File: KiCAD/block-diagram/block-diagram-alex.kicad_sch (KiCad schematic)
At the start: 34 parts, among them J1 Conn_01x08, J2 Conn_01x08, J3 Conn_01x10, Q3 NMOS, Q4 NMOS, U1 74LS02, U3 74LS11, U6 LMC555xM

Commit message: Grounded, open pin of the 555
There was a pin of the 555 that was connected to nothing, I connected it to ground, not sure if this is correct, but I believe generally that's what we are doing for unconnected pins, not sure if that one served a purpose though.
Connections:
- net GND: now also U6.5 (CV)
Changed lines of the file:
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@@
 	(wire
 		(pts
+			(xy 176.53 43.18) (xy 182.88 43.18)
+		)
+		(stroke
+			(width 0)
+			(type default)
+		)
+	)
+	(wire
+		(pts
 			(xy 115.57 102.87) (xy 215.9 102.87)
 		)
@@
 					(unit 1)
 				)
+			)
+		)
+	)
+	(symbol
+		(lib_id "power:GND")
+		(at 176.53 43.18 0)
+		(unit 1)
+		(exclude_from_sim no)
+		(in_bom yes)
+		(on_board yes)
+		(dnp no)
+		(fields_autoplaced yes)
+		(property "Reference" "#PWR029"
+			(at 176.53 49.53 0)
+			(effects
+				(font
+					(size 1.27 1.27)
+				)
+				(hide yes)
+			)
+		)
+		(property "Value" "GND"
+			(at 176.53 48.26 0)
+			(effects
+				(font
+					(size 1.27 1.27)
+				)
+			)
+		)
+		(property "Footprint" ""
+			(at 176.53 43.18 0)
+			(effects
+				(font
+					(size 1.27 1.27)
+				)
+				(hide yes)
+			)
+		)
+		(property "Datasheet" ""
+			(at 176.53 43.18 0)
+			(effects
+				(font
+					(size 1.27 1.27)
+				)
+				(hide yes)
+			)
+		)
+		(property "Description" "Power symbol creates a global label with name \"GND\" , ground"
+			(at 176.53 43.18 0)
+			(effects
+				(font
+					(size 1.27 1.27)
+				)
+				(hide yes)
+			)
+		)
+		(pin "1"
+		)
+		(instances
+			(project "block-diagram-alex"
+				(path "/db38bfac-663c-442a-8ac2-f7bf1aa9a3fd"
+					(reference "#PWR029")
+					(unit 1)
+				)

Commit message: Start filling symbol attributes; move J2 a bit
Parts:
- C4: CatNo (none) -> 4713-GMC21X5R106J10NTCT-ND; MfgNo (none) -> GMC21X5R106J10NT
- Q3, Q4: CatNo (none) -> DMN2046U-7DICT-ND; MfgNo (none) -> DMN2046U-7
- U6: CatNo (none) -> LM555CMX/NOPBCT-ND; MfgNo (none) -> LM555CMX/NOPB
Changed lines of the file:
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@@
 		(on_board yes)
 		(dnp no)
-		(fields_autoplaced yes)
 		(property "Reference" "U6"
 			(at 197.7741 30.48 0)
@@
 			)
 		)
+		(property "CatNo" "LM555CMX/NOPBCT-ND"
+			(at 180.848 53.086 0)
+			(effects
+				(font
+					(size 1.27 1.27)
+				)
+			)
+		)
+		(property "MfgNo" "LM555CMX/NOPB"
+			(at 195.58 43.18 0)
+			(effects
+				(font
+					(size 1.27 1.27)
+				)
+				(hide yes)
+			)
+		)
 		(pin "8"
 		)
@@
 			)
 		)
+		(property "CatNo" "DMN2046U-7DICT-ND"
+			(at 187.96 67.31 0)
+			(effects
+				(font
+					(size 1.27 1.27)
+				)
+				(hide yes)
+			)
+		)
+		(property "MfgNo" "DMN2046U-7"
+			(at 187.96 67.31 0)
+			(effects
+				(font
+					(size 1.27 1.27)
+				)
+				(hide yes)
+			)
+		)
 		(pin "1"
 		)
@@
 		(on_board yes)
 		(dnp no)
-		(fields_autoplaced yes)
 		(property "Reference" "C4"
 			(at 214.63 63.5062 0)
@@
 			)
 		)
+		(property "CatNo" "4713-GMC21X5R106J10NTCT-ND"
+			(at 230.378 68.58 0)
+			(effects
+				(font
+					(size 1.27 1.27)
+				)
+			)
+		)
+		(property "MfgNo" "GMC21X5R106J10NT"
+			(at 212.09 64.77 0)
+			(effects
+				(font
+					(size 1.27 1.27)
+				)
+				(hide yes)
+			)
+		)
 		(pin "2"
 		)
@@
 		(on_board yes)
 		(dnp no)
-		(fields_autoplaced yes)
 		(property "Reference" "Q3"
 			(at 173.99 66.0399 0)
@@
 			(effects
 				(font
+					(size 1.27 1.27)
+				)
+				(hide yes)
+			)
+		)
+		(property "CatNo" "DMN2046U-7DICT-ND"
+			(at 157.226 71.628 0)
+			(effects
+				(font
+					(size 1.27 1.27)
+				)
+			)
+		)
+		(property "MfgNo" "DMN2046U-7"
+			(at 167.64 67.31 0)
+			(effects
+				(font

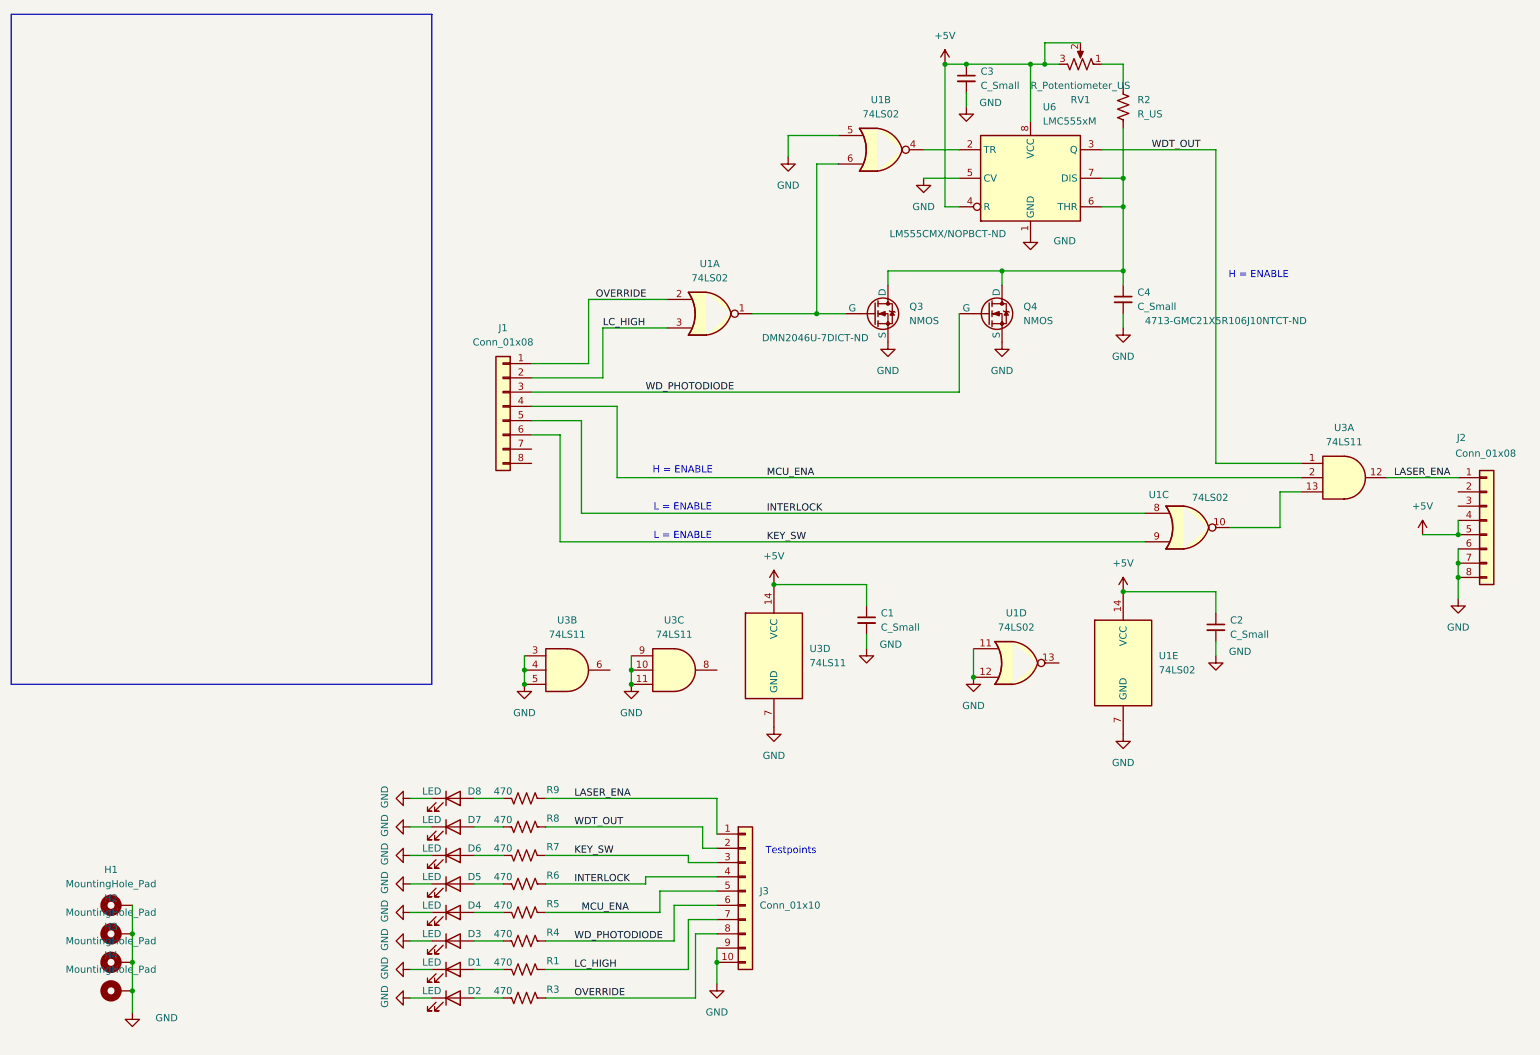
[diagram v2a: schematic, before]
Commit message: Finishing Touches before adding Part and Cfg Nums
*  Fix silkscreen text overlaps
*  Move J2 up or down .05" and fix routing
*  Disconnect 555 pin 5 from GND and add a 10uF capacitor
*  Change U1, U3 from 74LS--- to 74HC---
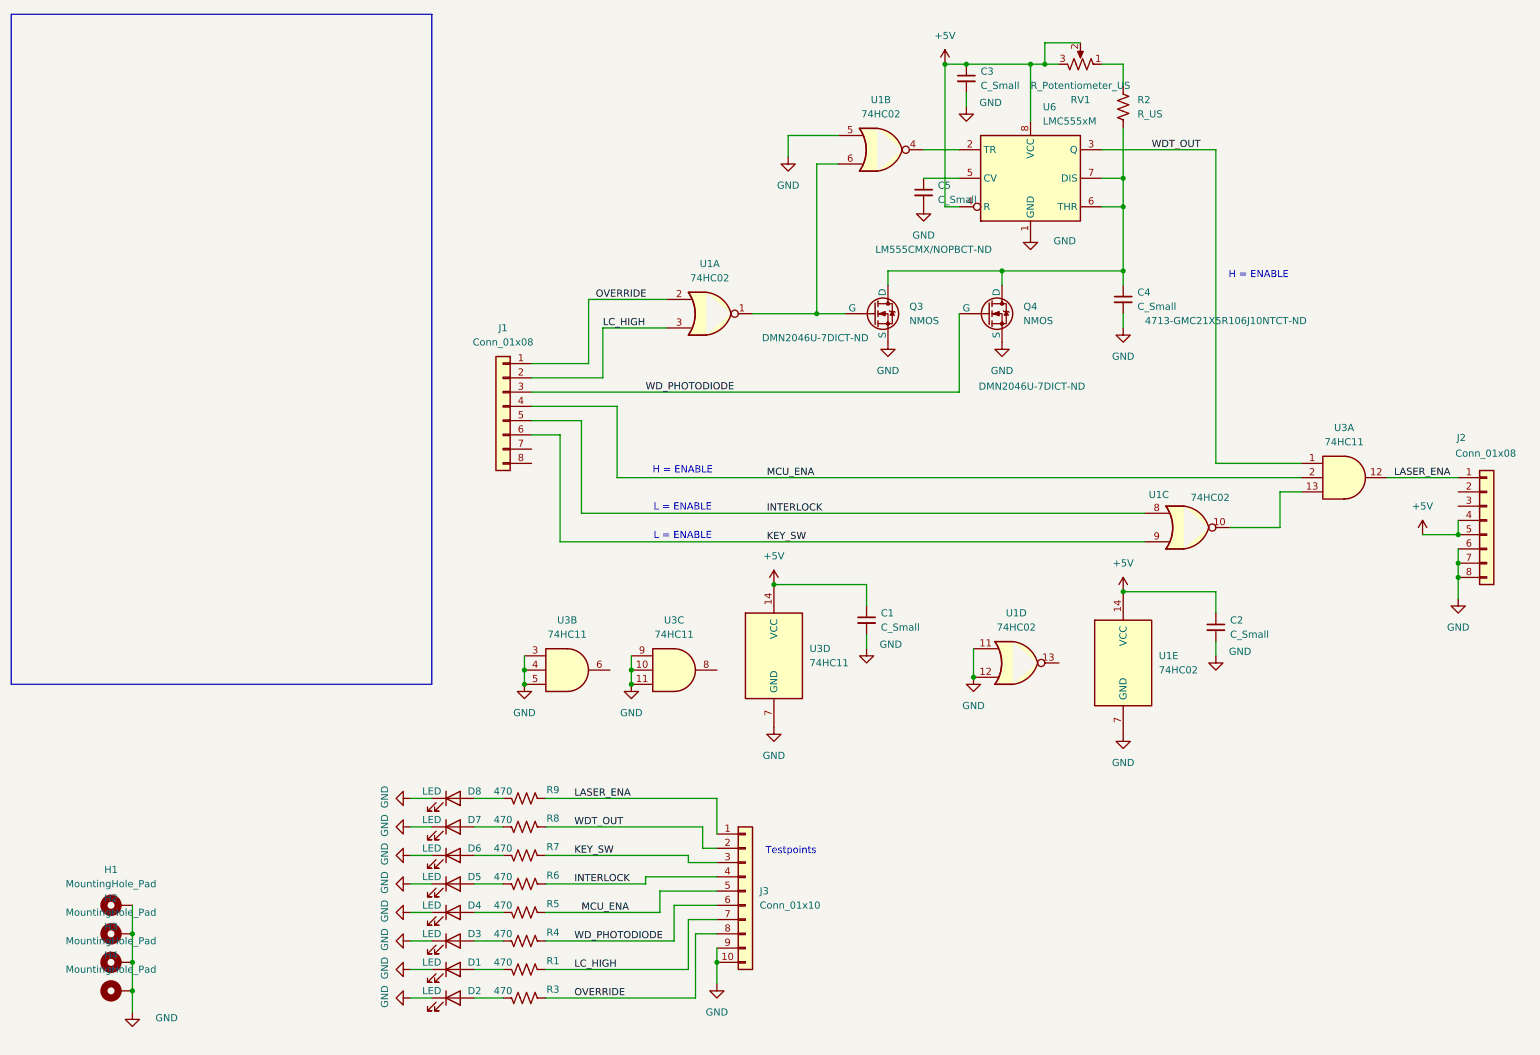
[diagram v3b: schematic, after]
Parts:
- added C5: C_Small, Capacitor_SMD:C_0805_2012Metric_Pad1.18x1.45mm_HandSolder, symbol Device:C_Small
- U1: value 74LS02 -> 74HC02
- U3: value 74LS11 -> 74HC11
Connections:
- net GND: now also C5.2; no longer U6.5 (CV)
- new net: C5.1, U6.5 (CV)
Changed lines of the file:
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@@
 			)
 		)
-		(property "Value" "74LS02"
+		(property "Value" "74HC02"
 			(at 168.91 31.75 0)
 			(effects
@@
 		)
 		(property "CatNo" "LM555CMX/NOPBCT-ND"
-			(at 180.848 53.086 0)
+			(at 178.308 55.88 0)
 			(effects
 				(font
@@
 			)
 		)
-		(property "Value" "74LS02"
+		(property "Value" "74HC02"
 			(at 227.584 100.076 0)
 			(effects
@@
 			)
 		)
-		(property "Value" "74LS02"
+		(property "Value" "74HC02"
 			(at 138.43 60.96 0)
 			(effects
@@
 			)
 		)
-		(property "Value" "74LS11"
+		(property "Value" "74HC11"
 			(at 132.0717 124.46 0)
 			(effects
@@
 	(symbol
 		(lib_id "Device:C_Small")
+		(at 176.53 45.72 0)
+		(unit 1)
+		(exclude_from_sim no)
+		(in_bom yes)
+		(on_board yes)
+		(dnp no)
+		(fields_autoplaced yes)
+		(property "Reference" "C5"
+			(at 179.07 44.4562 0)
+			(effects
+				(font
+					(size 1.27 1.27)
+				)
+				(justify left)
+			)
+		)
+		(property "Value" "C_Small"
+			(at 179.07 46.9962 0)
+			(effects
+				(font
+					(size 1.27 1.27)
+				)
+				(justify left)
+			)
+		)
+		(property "Footprint" "Capacitor_SMD:C_0805_2012Metric_Pad1.18x1.45mm_HandSolder"
+			(at 176.53 45.72 0)
+			(effects
+				(font
+					(size 1.27 1.27)
+				)
+				(hide yes)
+			)
+		)
+		(property "Datasheet" "~"
+			(at 176.53 45.72 0)
+			(effects
+				(font
+					(size 1.27 1.27)
+				)
+				(hide yes)
+			)
+		)
+		(property "Description" "Unpolarized capacitor, small symbol"
+			(at 176.53 45.72 0)
+			(effects
+				(font
+					(size 1.27 1.27)
+				)
+				(hide yes)
+			)
+		)
+		(pin "1"
+		)
+		(pin "2"
+		)
+		(instances
+			(project "block-diagram-alex"
+				(path "/db38bfac-663c-442a-8ac2-f7bf1aa9a3fd"
+					(reference "C5")
+					(unit 1)
+				)
+			)
+		)
+	)
+	(symbol
+		(lib_id "Device:C_Small")
 		(at 228.6 123.19 0)
 		(unit 1)
@@
 	(symbol
 		(lib_id "power:GND")
-		(at 176.53 43.18 0)
+		(at 176.53 48.26 0)
 		(unit 1)
 		(exclude_from_sim no)
@@
 		(fields_autoplaced yes)
 		(property "Reference" "#PWR029"
-			(at 176.53 49.53 0)
+			(at 176.53 54.61 0)
 			(effects
 				(font
@@
 		)
 		(property "Value" "GND"
-			(at 176.53 48.26 0)
+			(at 176.53 53.34 0)
 			(effects
 				(font
@@
 		)
 		(property "Footprint" ""
-			(at 176.53 43.18 0)
+			(at 176.53 48.26 0)
 			(effects
 				(font
@@
 		)
 		(property "Datasheet" ""
-			(at 176.53 43.18 0)
+			(at 176.53 48.26 0)
 			(effects
 				(font
@@
 		)
 		(property "Description" "Power symbol creates a global label with name \"GND\" , ground"
-			(at 176.53 43.18 0)
+			(at 176.53 48.26 0)
 			(effects
 				(font
@@
 			)
 		)
-		(property "Value" "74LS02"
+		(property "Value" "74HC02"
 			(at 193.04 123.19 0)
 			(effects
@@
 			)
 		)
-		(property "Value" "74LS02"
+		(property "Value" "74HC02"
 			(at 218.44 130.8099 0)
 			(effects
@@
 			)
 		)
-		(property "Value" "74LS11"
+		(property "Value" "74HC11"
 			(at 251.4517 90.17 0)
 			(effects
@@
 		(on_board yes)
 		(dnp no)
-		(fields_autoplaced yes)
 		(property "Reference" "Q4"
 			(at 194.31 66.0399 0)
@@
 		)
 		(property "CatNo" "DMN2046U-7DICT-ND"
-			(at 187.96 67.31 0)
+			(at 195.834 80.264 0)
 			(effects
 				(font
 					(size 1.27 1.27)
 				)
-				(hide yes)
 			)
 		)
@@
 			)
 		)
-		(property "Value" "74LS11"
+		(property "Value" "74HC11"
 			(at 113.0217 124.46 0)
 			(effects
@@
 			)
 		)
-		(property "Value" "74LS11"
+		(property "Value" "74HC11"
 			(at 156.21 129.5399 0)
 			(effects

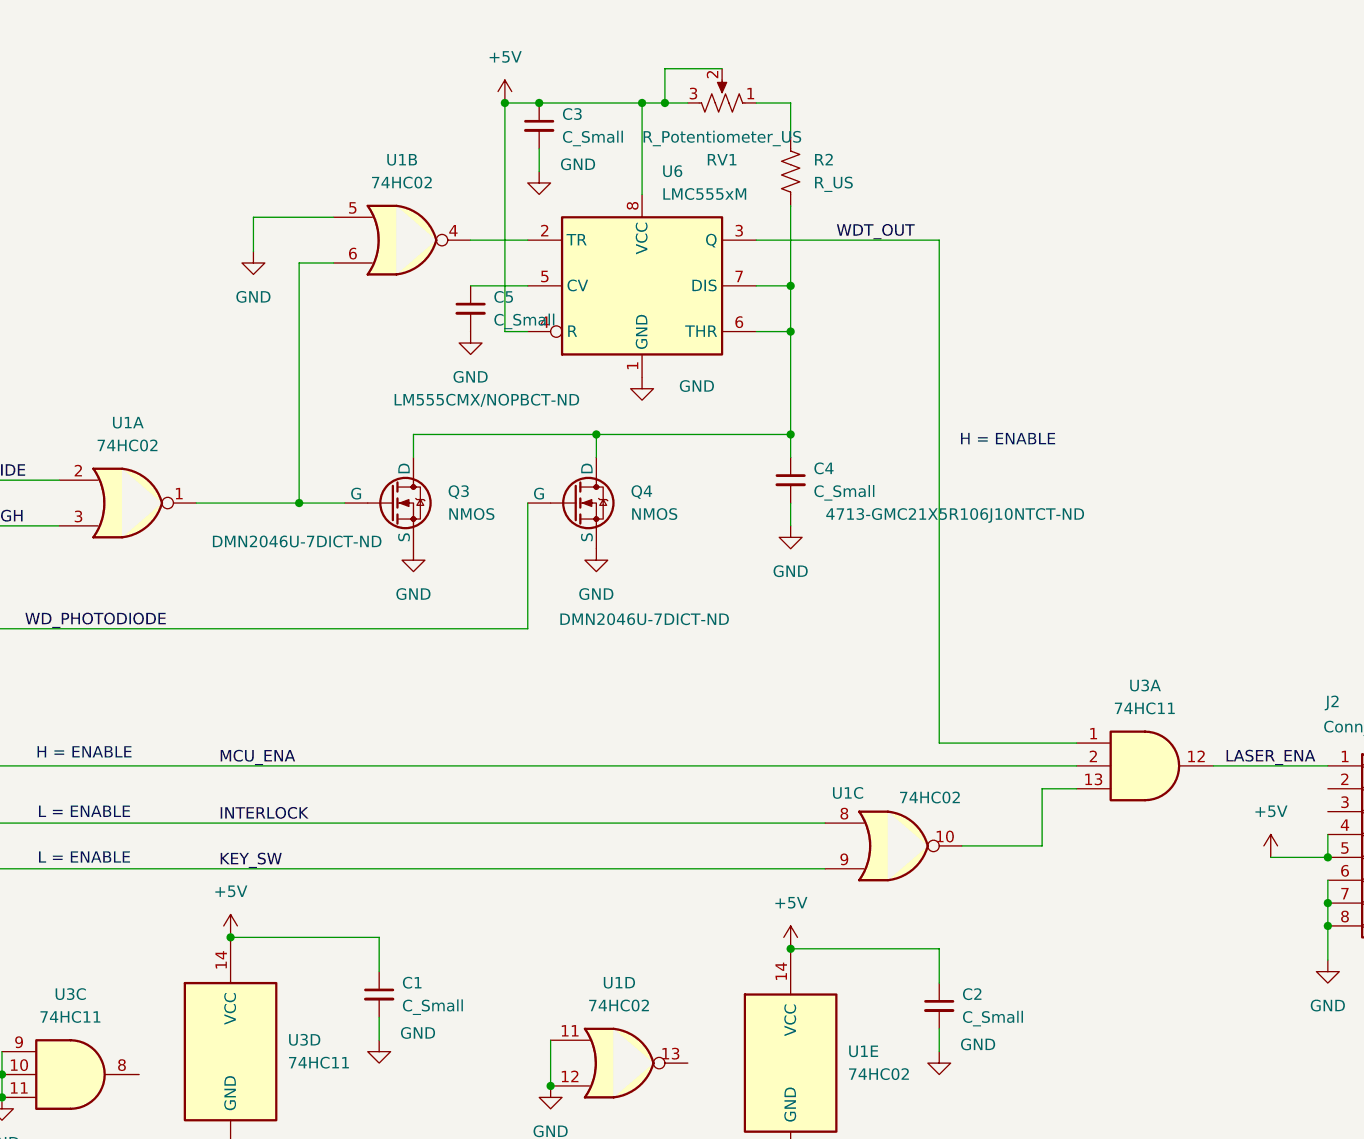
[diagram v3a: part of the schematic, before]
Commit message: Capacitor CatNo and CfgNo
Added part and cfg numbers for remaining capacitors, all are 10 nf.
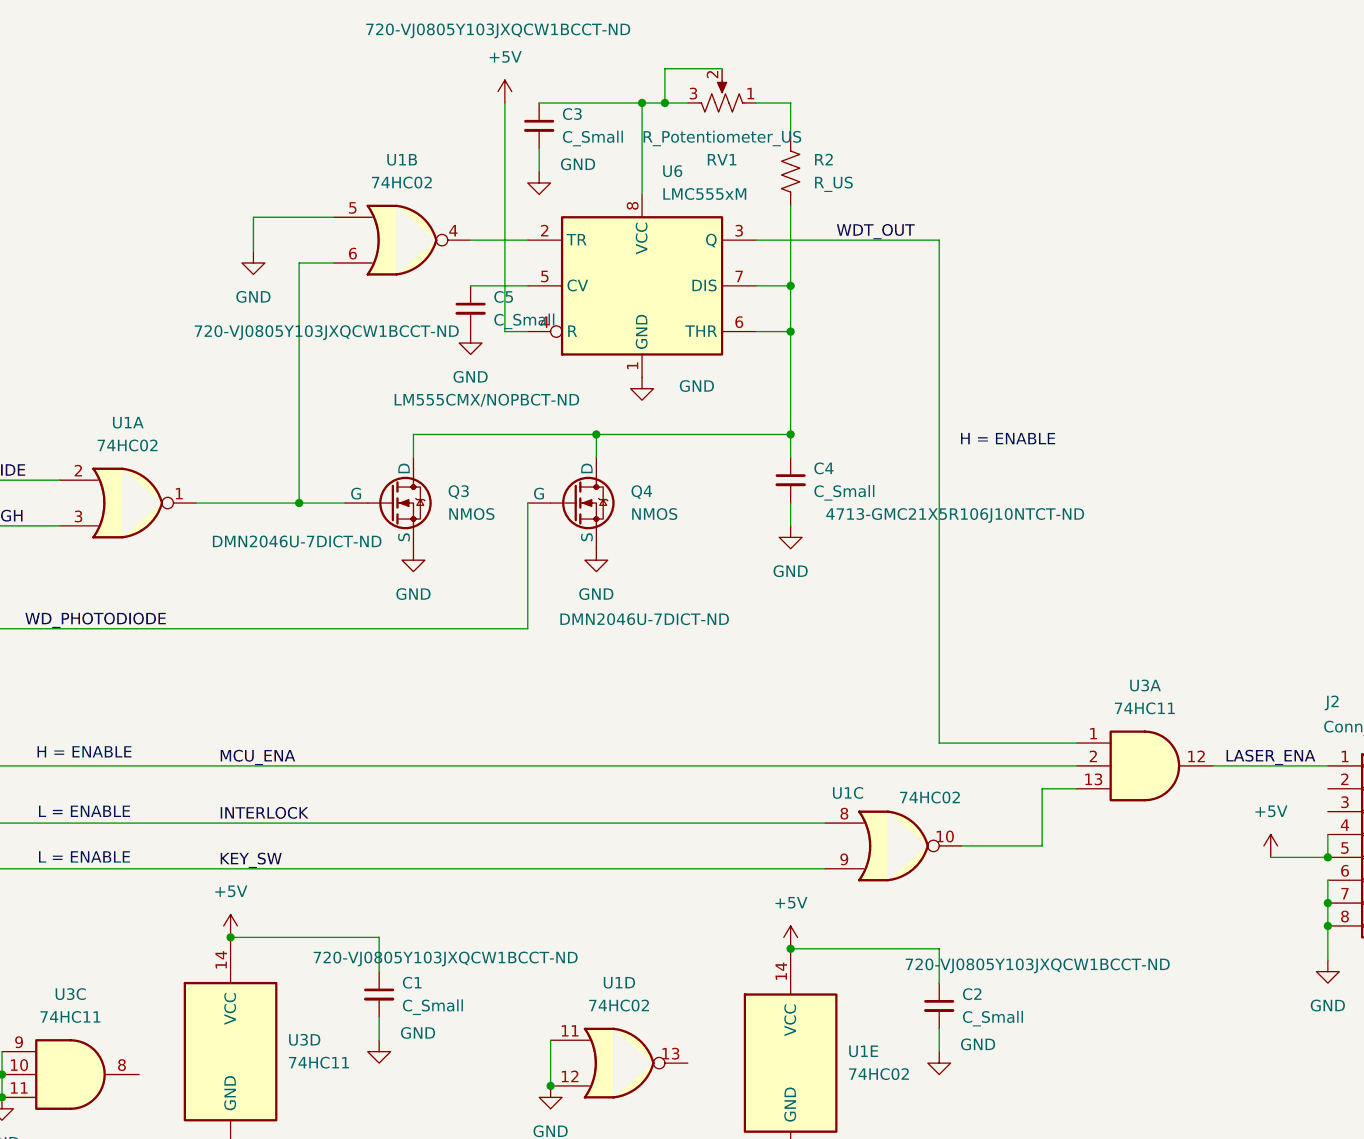
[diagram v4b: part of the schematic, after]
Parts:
- C1, C2, C3, C5: CatNo (none) -> 720-VJ0805Y103JXQCW1BCCT-ND; MfgNo (none) -> VJ0805Y103JXQCW1BC
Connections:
- net +5V: no longer C3.1, RV1.2, RV1.3, U6.8 (VCC)
- new net: C3.1, RV1.2, RV1.3, U6.8 (VCC)
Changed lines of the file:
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@@
 	)
 	(junction
-		(at 180.34 22.86)
-		(diameter 0)
-		(color 0 0 0 0)
-	)
-	(junction
-		(at 184.15 22.86)
-		(diameter 0)
-		(color 0 0 0 0)
-	)
-	(junction
 		(at 124.46 130.81)
 		(diameter 0)
@@
 	(wire
 		(pts
-			(xy 180.34 22.86) (xy 184.15 22.86)
-		)
-		(stroke
-			(width 0)
-			(type default)
-		)
-	)
-	(wire
-		(pts
 			(xy 132.08 179.07) (xy 132.08 172.72)
 		)
@@
 		(on_board yes)
 		(dnp no)
-		(fields_autoplaced yes)
 		(property "Reference" "C1"
 			(at 168.91 120.6562 0)
@@
 			)
 		)
+		(property "CatNo" "720-VJ0805Y103JXQCW1BCCT-ND"
+			(at 173.736 117.856 0)
+			(effects
+				(font
+					(size 1.27 1.27)
+				)
+			)
+		)
+		(property "MfgNo" "VJ0805Y103JXQCW1BC"
+			(at 166.37 121.92 0)
+			(effects
+				(font
+					(size 1.27 1.27)
+				)
+				(hide yes)
+			)
+		)
 		(pin "2"
 		)
@@
 		(on_board yes)
 		(dnp no)
-		(fields_autoplaced yes)
 		(property "Reference" "C3"
 			(at 186.69 24.1362 0)
@@
 			)
 		)
+		(property "CatNo" "720-VJ0805Y103JXQCW1BCCT-ND"
+			(at 179.578 14.732 0)
+			(effects
+				(font
+					(size 1.27 1.27)
+				)
+			)
+		)
+		(property "MfgNo" "VJ0805Y103JXQCW1BC"
+			(at 184.15 25.4 0)
+			(effects
+				(font
+					(size 1.27 1.27)
+				)
+				(hide yes)
+			)
+		)
 		(pin "2"
 		)
@@
 		(on_board yes)
 		(dnp no)
-		(fields_autoplaced yes)
 		(property "Reference" "C5"
 			(at 179.07 44.4562 0)
@@
 			)
 		)
+		(property "CatNo" "720-VJ0805Y103JXQCW1BCCT-ND"
+			(at 160.528 48.26 0)
+			(effects
+				(font
+					(size 1.27 1.27)
+				)
+			)
+		)
+		(property "MfgNo" "VJ0805Y103JXQCW1BC"
+			(at 176.53 45.72 0)
+			(effects
+				(font
+					(size 1.27 1.27)
+				)
+				(hide yes)
+			)
+		)
 		(pin "1"
 		)
@@
 		(on_board yes)
 		(dnp no)
-		(fields_autoplaced yes)
 		(property "Reference" "C2"
 			(at 231.14 121.9262 0)
@@
 			(at 228.6 123.19 0)
 			(effects
+				(font
+					(size 1.27 1.27)
+				)
+				(hide yes)
+			)
+		)
+		(property "CatNo" "720-VJ0805Y103JXQCW1BCCT-ND"
+			(at 239.522 118.618 0)
+			(effects
+				(font
+					(size 1.27 1.27)
+				)
+			)
+		)
+		(property "MfgNo" "VJ0805Y103JXQCW1BC"
+			(at 228.6 123.19 0)
+			(effects
